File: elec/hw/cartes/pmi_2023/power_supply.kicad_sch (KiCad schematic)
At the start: 53 parts, among them J5 254, J8 254, Q3 DMP2008UFG-7, SW8 MSS12C02LS-BB2.0, U28 TLV61070A, U29 TLV61070A, U33 TLV61070A, U34 TLV61070A, U35 LDL1117S33R

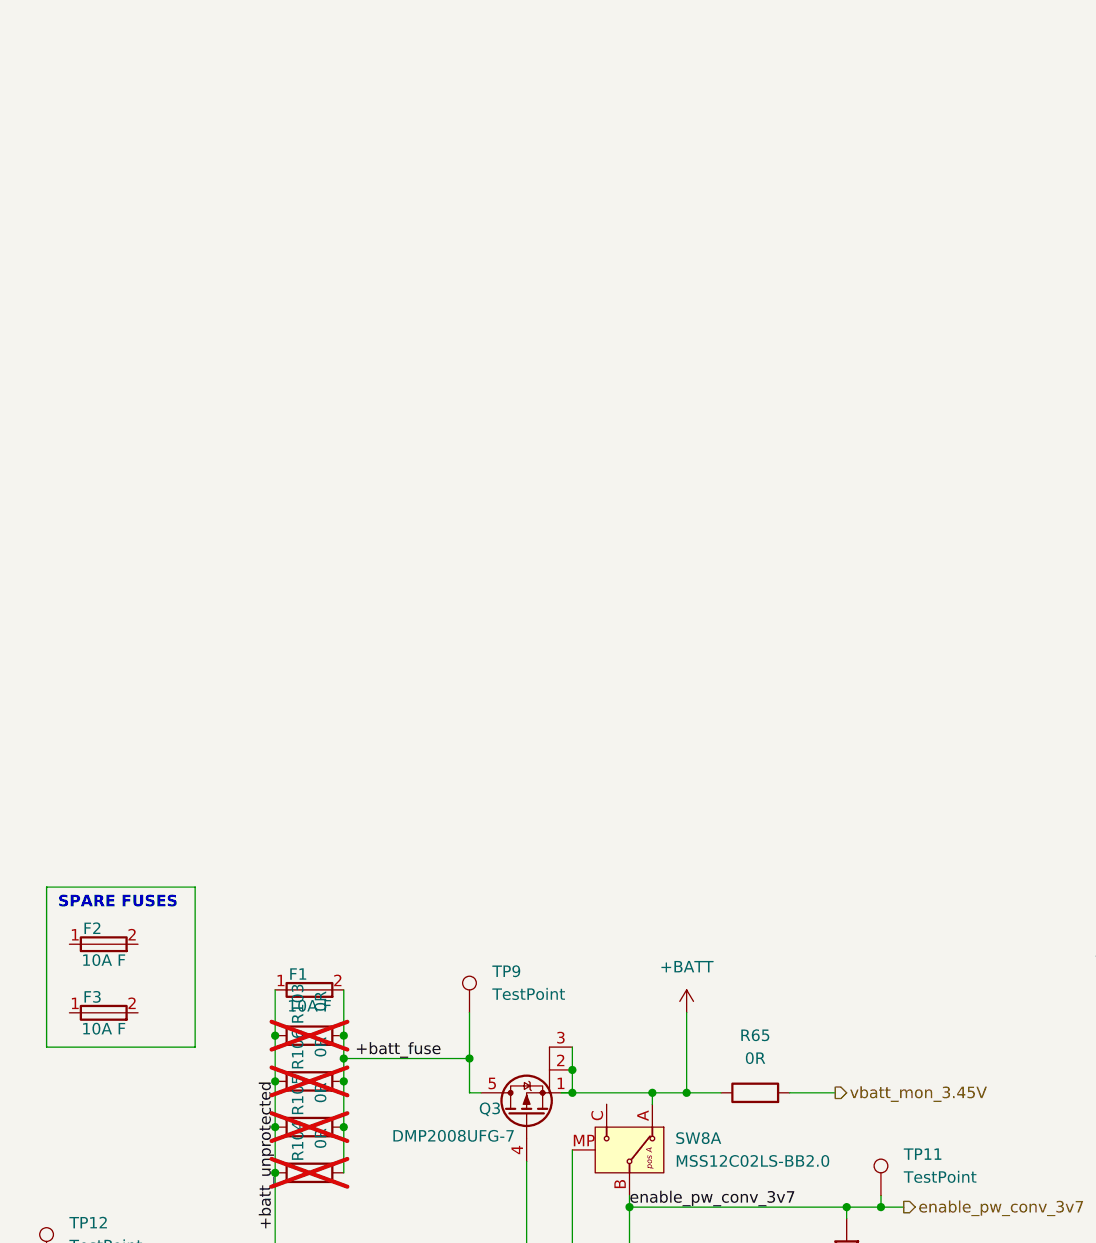
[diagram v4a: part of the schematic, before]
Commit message: pmi: beginning of transition toward 0402 resistors and capacitors, battery gauge added
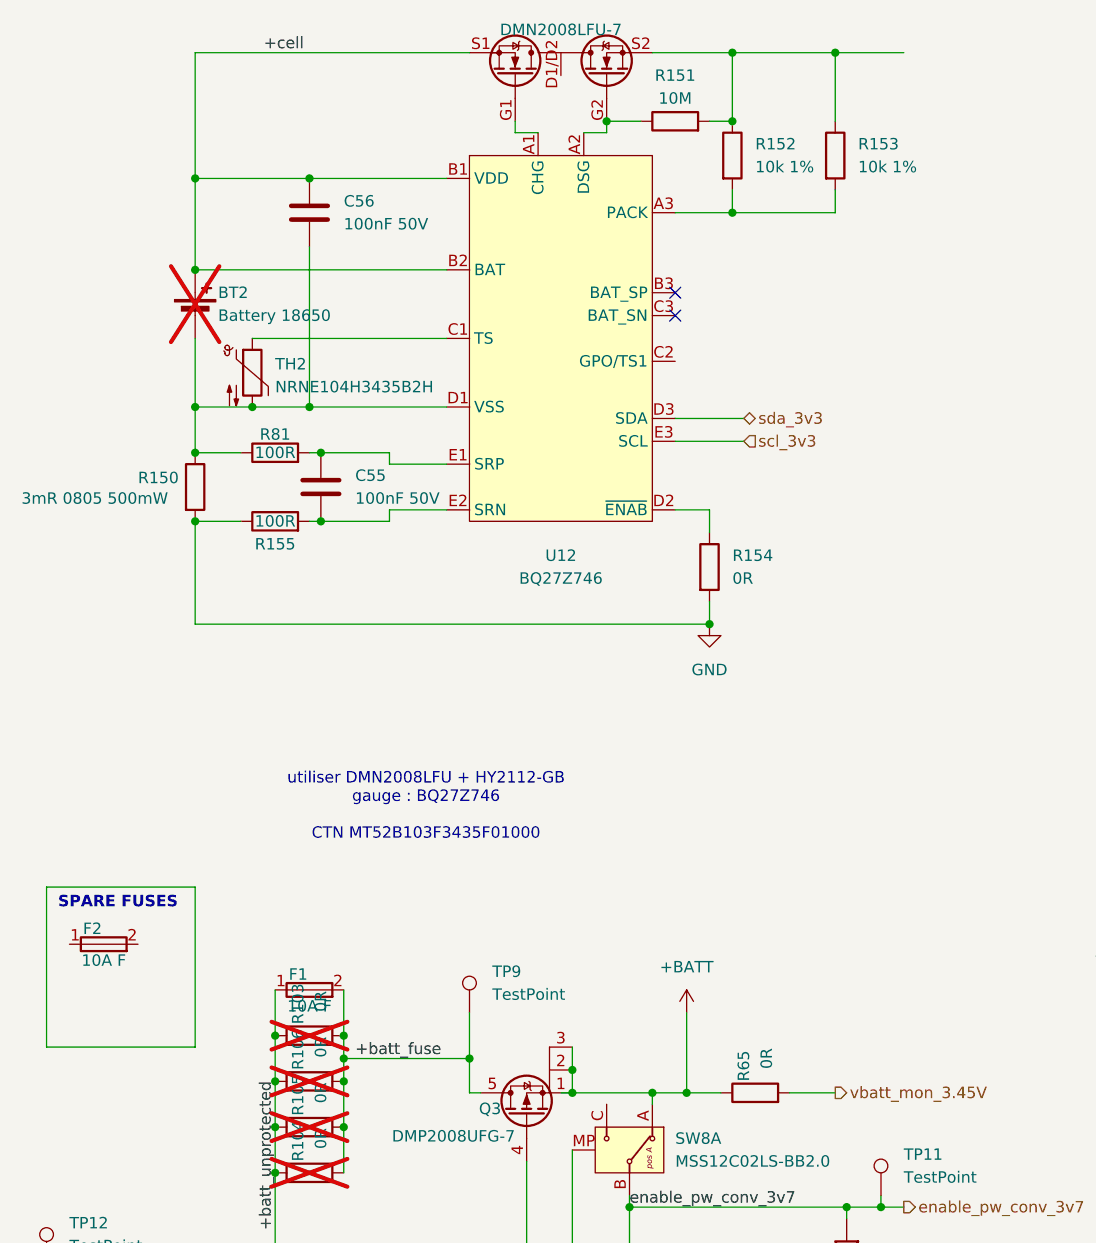
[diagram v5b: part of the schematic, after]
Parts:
- removed F3: 10A F, cocotter_others:JFC2410, symbol cocotter_others:JFC2410-2100FS
- added BT2: Battery 18650, symbol cocotter_others:Battery_Cell-18650
- added C55, C56: 100nF 50V, cocotter_capacitors:C_0402_1005Metric, symbol cocotter_capacitors:C_100nF_50V_0402
- added Q2: DMN2008LFU-7, cocotter_transistors:U-DFN2030-6, symbol cocotter_transistors:DMN2008LFU-7
- added R150: 3mR 0805 500mW, cocotter_resistor:PA0805, symbol cocotter_resistors:R_3mR_0805_1%
- added R151: 10M, cocotter_resistor:r0402_reflow, symbol cocotter_resistors:R_10M_0402_1%
- added R152, R153: 10k 1%, cocotter_resistor:r0402_reflow, symbol cocotter_resistors:R_10k_0402_1%
- added R154: 0R, cocotter_resistor:r0402_reflow, symbol cocotter_resistors:R_0R_0402
- added R155, R81: 100R, cocotter_resistor:r0402_reflow, symbol cocotter_resistors:R_100R_0402_1%
- added TH2: NRNE104H3435B2H, cocotter_resistor:CTN-NRN, symbol cocotter_resistors:NRNE104H3435B2H
- added U12: BQ27Z746, cocotter_ic:YAH0015, symbol cocotter_ic:BQ27Z746
- R107, R108, R111, R113: footprint cocotter_resistor:r0603_reflow -> cocotter_resistor:r0402_reflow; symbol cocotter_resistors:R_10k_0603_1% -> cocotter_resistors:R_10k_0402_1%; JLCPCB Part # C25804 -> C; Specification 10k 0603 1% 100mW -> 10k 0402 1% 100mW
- R65: footprint cocotter_resistor:r0603_reflow -> cocotter_resistor:r0402_reflow; symbol cocotter_resistors:R_0R_0603 -> cocotter_resistors:R_0R_0402; JLCPCB Part # C431718 -> C; Specification 0R 0603 20mOhms max 100mW -> 0R 0603
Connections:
- net GND: now also R150.2, R154.2, R155.1
- new net: BT2.2 (-), C56.2, R150.1, R81.1, TH2.2, U12.D1 (VSS)
- new net: C55.1, R81.2, U12.E1 (SRP)
- new net: C55.2, R155.2, U12.E2 (SRN)
- new net: Q2.G1, U12.A1 (CHG)
- new net: Q2.G2, R151.1, U12.A2 (DSG)
- new net: R152.2, R153.2, U12.A3 (PACK)
- new net: TH2.1, U12.C1 (TS)
- new net: R154.1, U12.D2 (~{ENAB})
- new net: Q2.S2, R151.2, R152.1, R153.1
- new net +cell: BT2.1 (+), C56.1, Q2.S1 (S), U12.B1 (VDD), U12.B2 (BAT)
- new net scl_3v3: U12.E3 (SCL)
- new net sda_3v3: U12.D3 (SDA)
- no-connect marks 0 -> 2
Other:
- note added: "utiliser DMN2008LFU + HY2112-GB gauge : BQ27Z746 CTN MT52B103F3435F01000"

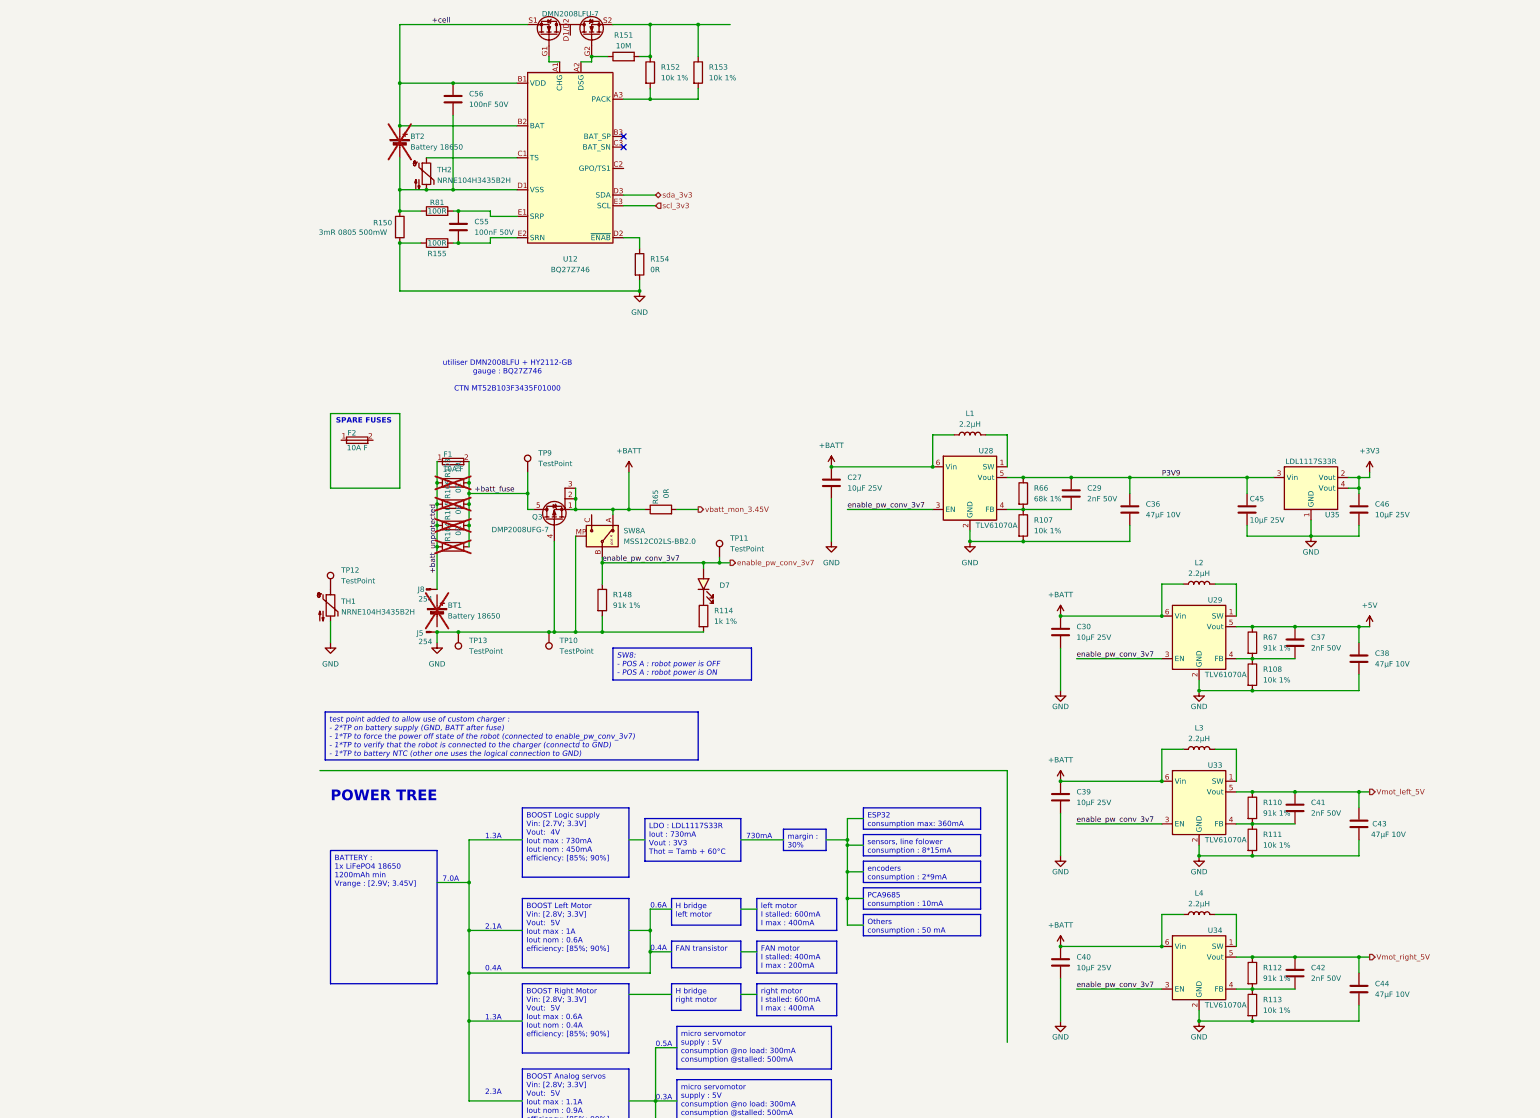
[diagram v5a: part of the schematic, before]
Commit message: pmi2023 : gauge routing done
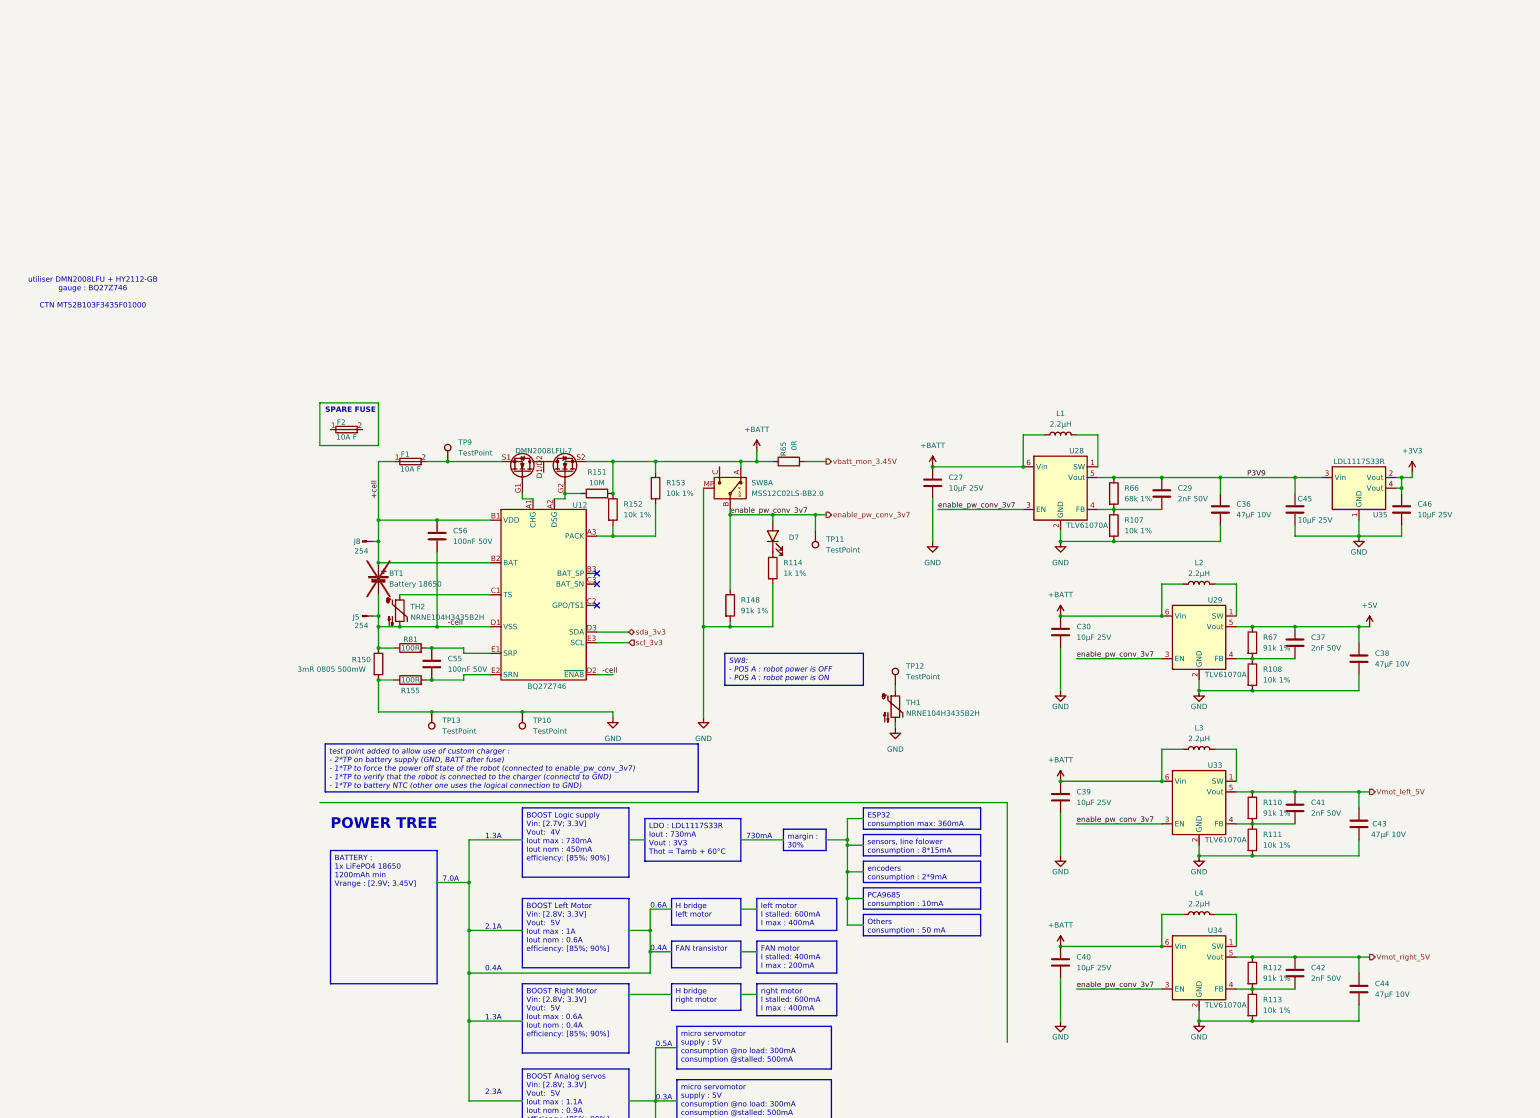
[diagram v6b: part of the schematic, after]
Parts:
- removed BT2: Battery 18650, symbol cocotter_others:Battery_Cell-18650
- removed Q3: DMP2008UFG-7, cocotter_transistors:Diodes_PowerDI3333-8, symbol cocotter_transistors:DMP2008UFG-7
- removed R103, R104, R105, R106: 0R, cocotter_resistor:r0603_reflow, symbol cocotter_resistors:R_0R_0603
- removed R154: 0R, cocotter_resistor:r0402_reflow, symbol cocotter_resistors:R_0R_0402
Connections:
- net +batt_unprotected is gone; now on net +cell: F1.1, J8.1 (GND)
- net +BATT: now also Q2.S2, R151.2, R152.1, R153.1
- net +cell: now also BT1.1 (+); no longer Q2.S1 (S)
- net GND: no longer J5.1 (GND)
- net -cell: now reaches C56.2, R150.1, R81.1, TH2.2, U12.D1 (VSS)
- net -cell: now also BT1.2 (-), J5.1 (GND), U12.D2 (~{ENAB})
- net +batt_fuse: no longer names the net of F1.2, TP9.1
- net +batt_fuse: now also Q2.S1 (S)
- no-connect marks 2 -> 3
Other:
- note added: "SPARE FUSE"
- note removed: "SPARE FUSES"
- moved on the sheet: BT1, C27, C29, C36, C45, C46, C55, C56, D7, F1, F2, J5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

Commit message: pmi2023 updated
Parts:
- added TP21: TestPoint, cocotter_others:testpoint-THT-0.5mm, symbol cocotter_others:TestPoint_for_pogo_pin-1mm
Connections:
- net -cell: now also TP21.1
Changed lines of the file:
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@@
 	)
 	(junction
+		(at 26.67 69.85)
+		(diameter 0)
+		(color 0 0 0 0)
+	)
+	(junction
 		(at 213.36 30.48)
 		(diameter 0)
@@
 	(wire
 		(pts
-			(xy 26.67 66.04) (xy 26.67 71.12)
+			(xy 26.67 69.85) (xy 26.67 71.12)
+		)
+		(stroke
+			(width 0)
+			(type default)
+		)
+	)
+	(wire
+		(pts
+			(xy 26.67 66.04) (xy 26.67 69.85)
 		)
 		(stroke
@@
 	(symbol
 		(lib_id "cocotter_others:TestPoint_for_pogo_pin-1mm")
+		(at 26.67 69.85 90)
+		(unit 1)
+		(exclude_from_sim no)
+		(in_bom no)
+		(on_board yes)
+		(dnp no)
+		(property "Reference" "TP21"
+			(at 19.304 68.834 90)
+			(effects
+				(font
+					(size 1.27 1.27)
+				)
+			)
+		)
+		(property "Value" "TestPoint"
+			(at 17.78 70.612 90)
+			(effects
+				(font
+					(size 1.27 1.27)
+				)
+			)
+		)
+		(property "Footprint" "cocotter_others:testpoint-THT-0.5mm"
+			(at 26.67 64.77 0)
+			(effects
+				(font
+					(size 1.27 1.27)
+				)
+				(hide yes)
+			)
+		)
+		(property "Datasheet" "~"
+			(at 26.67 64.77 0)
+			(effects
+				(font
+					(size 1.27 1.27)
+				)
+				(hide yes)
+			)
+		)
+		(property "Description" "test point"
+			(at 26.67 69.85 0)
+			(effects
+				(font
+					(size 1.27 1.27)
+				)
+				(hide yes)
+			)
+		)
+		(property "JLCPCB" ""
+			(at 26.67 69.85 0)
+			(effects
+				(font
+					(size 1.27 1.27)
+				)
+				(hide yes)
+			)
+		)
+		(property "Sim.Device" ""
+			(at 26.67 69.85 0)
+			(effects
+				(font
+					(size 1.27 1.27)
+				)
+				(hide yes)
+			)
+		)
+		(property "Sim.Pins" ""
+			(at 26.67 69.85 0)
+			(effects
+				(font
+					(size 1.27 1.27)
+				)
+				(hide yes)
+			)
+		)
+		(property "specification" ""
+			(at 26.67 69.85 0)
+			(effects
+				(font
+					(size 1.27 1.27)
+				)
+				(hide yes)
+			)
+		)
+		(pin "1"
+		)
+		(instances
+			(project "pmi_2023"
+				(path "/334a657f-c66c-4260-9567-14f1c99913d7/5ea42701-5087-46e6-be28-1d7732af67f5"
+					(reference "TP21")
+					(unit 1)
+				)
+			)
+		)
+	)
+	(symbol
+		(lib_id "cocotter_others:TestPoint_for_pogo_pin-1mm")
 		(at 130.81 43.18 180)
 		(unit 1)
@@
 		(on_board yes)
 		(dnp no)
-		(fields_autoplaced yes)
 		(property "Reference" "TH2"
-			(at 34.29 61.2774 0)
+			(at 34.29 60.198 0)
 			(effects
 				(font
@@
 		)
 		(property "Value" "NRNE104H3435B2H"
-			(at 34.29 63.8174 0)
+			(at 34.29 62.484 0)
 			(effects
 				(font

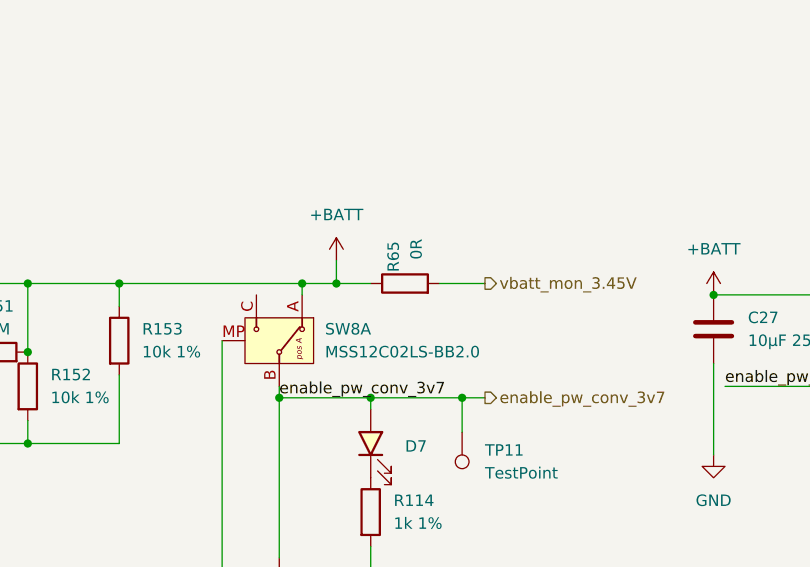
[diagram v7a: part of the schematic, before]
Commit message: pmi2023 : routing updated
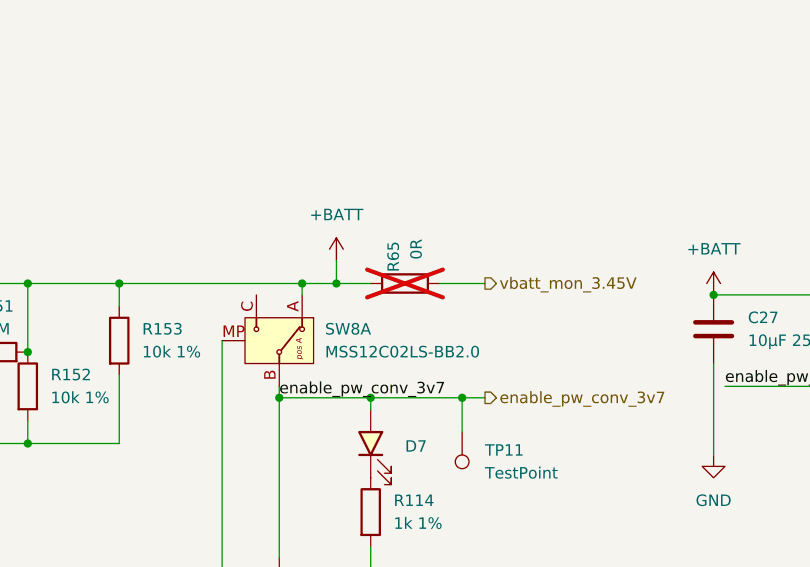
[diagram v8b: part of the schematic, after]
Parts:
- R65: now not fitted
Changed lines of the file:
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@@
 		(in_bom yes)
 		(on_board yes)
-		(dnp no)
+		(dnp yes)
 		(property "Reference" "R65"
 			(at 123.19 25.4 0)
